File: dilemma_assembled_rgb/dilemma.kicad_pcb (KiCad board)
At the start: 2 copper layers, 106.1 x 95.1 mm, 121 parts, among them J1 USB_C_Receptacle_USB2.0, J102 Serial, J105 Conn_01x04_Female, J113 Cirque, J2 Conn_01x03_Female, J5 Conn_01x02, SW1 SW_Push, SW110 SW_SPST, SW2 SW_Push, SW3002 RotaryEncoder_Switch, U1 RP2040, U2 GD25Q80CEIGR, U3 XC6210B332MR-G, U4 USBLC6-2P6, Y1 Crystal_GND24

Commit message: bat54
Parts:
- added D3: SK6805-EC15, 0xB2_drawings:LED_SK6805-EC15_hole, F.Cu at (137.7, 36.2)
- D101, D102, D103, D104, D105, D106, D107, D108, D109, D110, D111, D112, D113, D114, D115, D116, D117, D3001: footprint Diode_SMD:D_SOD-323 -> local-libraries:D_1206_handsolder_reversible_hole
- J113: moved to B.Cu
- moved J113 22.5 mm to (131.5, 93.6), turned to -90 degrees

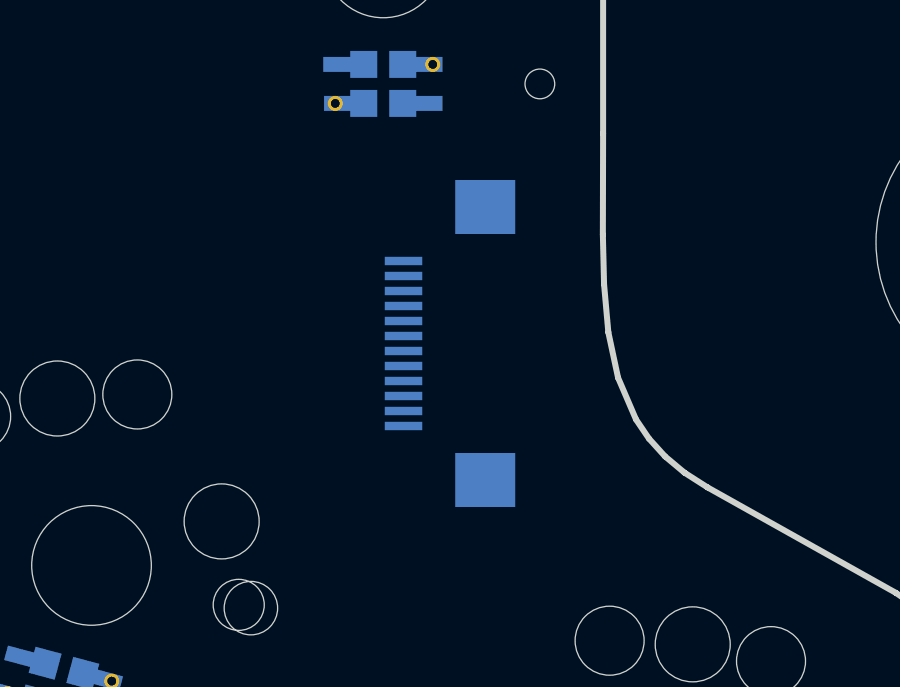
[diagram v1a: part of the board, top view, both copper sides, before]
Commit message: switch rgb to smd connectors
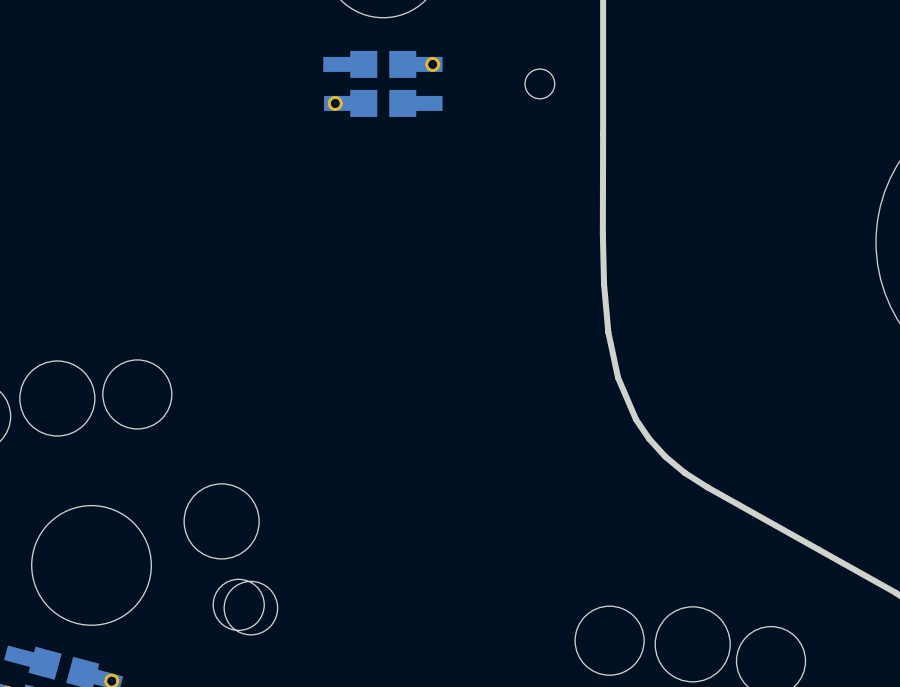
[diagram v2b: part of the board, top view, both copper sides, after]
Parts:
- removed J113: Cirque, local-libraries:FPC-SMD_FPC05012-09200-.5mm

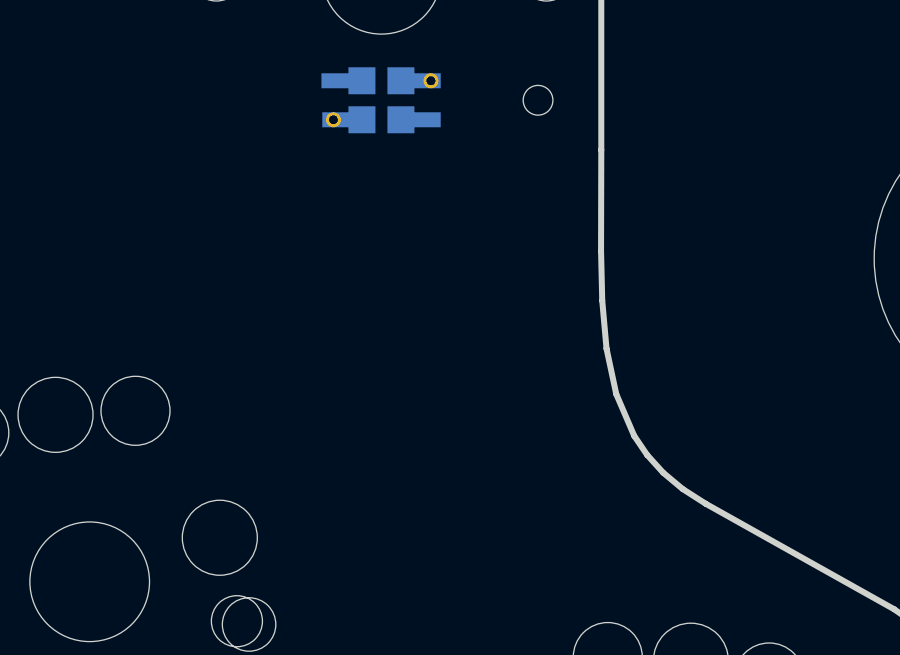
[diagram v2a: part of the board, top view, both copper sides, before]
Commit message: flip debug headers
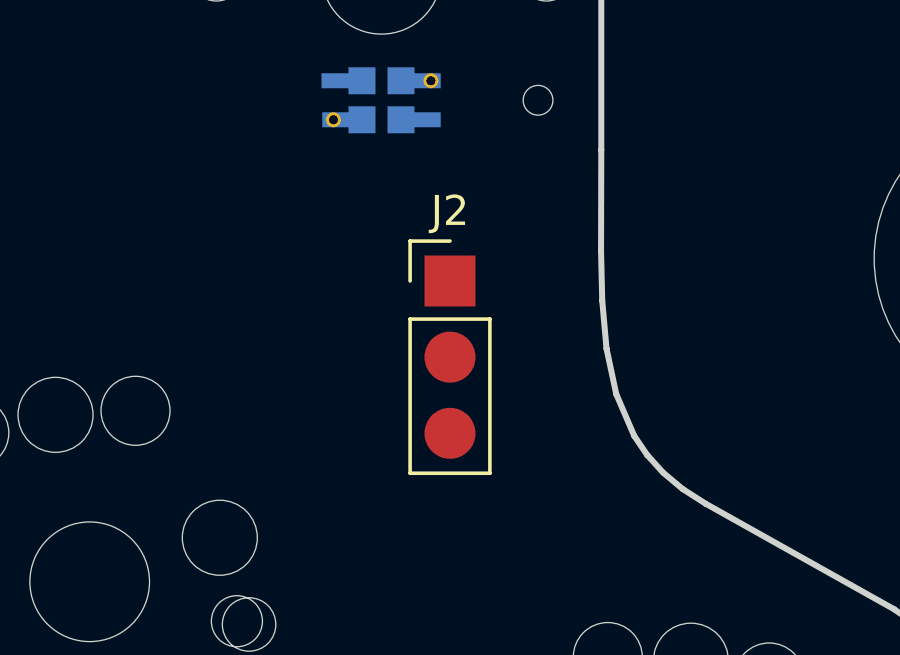
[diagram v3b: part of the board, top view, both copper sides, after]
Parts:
- added J2: Conn_01x03_Female, local-libraries:PinHeader_1x03_P2.54mm_Vertical_smd, F.Cu at (131.7, 91.0)
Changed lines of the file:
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@@
     (fp_line (start 1.3 -0.2) (end 1.3 7.75) (layer "B.SilkS") (width 0.12))
     (fp_line (start -1.299921 -0.198003) (end -1.299921 7.751997) (layer "B.SilkS") (width 0.12))
-    (fp_arc (start -1.299921 -0.198003) (mid -0.00092 -1.448967) (end 1.3 -0.2) (layer "B.SilkS") (width 0.12))
-    (fp_arc (start 1.3 7.75) (mid 0.000999 9.000965) (end -1.299921 7.751997) (layer "B.SilkS") (width 0.12))
+    (fp_arc (start -1.299921 -0.198003) (mid -0.00092 -1.448968) (end 1.3 -0.2) (layer "B.SilkS") (width 0.12))
+    (fp_arc (start 1.3 7.75) (mid 0.000999 9.000966) (end -1.299921 7.751997) (layer "B.SilkS") (width 0.12))
     (fp_line (start 1.314577 -0.199039) (end 1.314577 7.751997) (layer "F.SilkS") (width 0.12))
     (fp_line (start -1.285344 -0.201036) (end -1.285344 7.75) (layer "F.SilkS") (width 0.12))
@@
     (pad "" np_thru_hole oval (at 0 0 180) (size 6.5 3) (drill oval 6.5 3) (layers F&B.Cu *.Mask))
   )
+  (footprint "local-libraries:PinHeader_1x03_P2.54mm_Vertical_smd" (layer "F.Cu")
+    (at 131.71 90.97)
+    (descr "Through hole straight pin header, 1x03, 2.54mm pitch, single row")
+    (tags "Through hole pin header THT 1x03 2.54mm single row")
+    (property "Sheetfile" "dilemma.kicad_sch")
+    (property "Sheetname" "")
+    (attr through_hole)
+    (fp_text reference "J2" (at 0 -2.33) (layer "F.SilkS")
+      (effects (font (size 1 1) (thickness 0.15)))
+    )
+    (fp_text value "Conn_01x03_Female" (at 0 7.41) (layer "F.Fab")
+      (effects (font (size 1 1) (thickness 0.15)))
+    )
+    (fp_text user "${REFERENCE}" (at 0 2.54 90) (layer "F.Fab")
+      (effects (font (size 1 1) (thickness 0.15)))
+    )
+    (fp_line (start -1.33 6.41) (end 1.33 6.41) (layer "F.SilkS") (width 0.12))
+    (fp_line (start -1.33 0) (end -1.33 -1.33) (layer "F.SilkS") (width 0.12))
+    (fp_line (start -1.33 1.27) (end -1.33 6.41) (layer "F.SilkS") (width 0.12))
+    (fp_line (start -1.33 1.27) (end 1.33 1.27) (layer "F.SilkS") (width 0.12))
+    (fp_line (start -1.33 -1.33) (end 0 -1.33) (layer "F.SilkS") (width 0.12))
+    (fp_line (start 1.33 1.27) (end 1.33 6.41) (layer "F.SilkS") (width 0.12))
+    (fp_line (start -1.8 6.85) (end 1.8 6.85) (layer "F.CrtYd") (width 0.05))
+    (fp_line (start -1.8 -1.8) (end -1.8 6.85) (layer "F.CrtYd") (width 0.05))
+    (fp_line (start 1.8 -1.8) (end -1.8 -1.8) (layer "F.CrtYd") (width 0.05))
+    (fp_line (start 1.8 6.85) (end 1.8 -1.8) (layer "F.CrtYd") (width 0.05))
+    (fp_line (start -0.635 -1.27) (end 1.27 -1.27) (layer "F.Fab") (width 0.1))
+    (fp_line (start -1.27 -0.635) (end -0.635 -1.27) (layer "F.Fab") (width 0.1))
+    (fp_line (start 1.27 6.35) (end -1.27 6.35) (layer "F.Fab") (width 0.1))
+    (fp_line (start 1.27 -1.27) (end 1.27 6.35) (layer "F.Fab") (width 0.1))
+    (fp_line (start -1.27 6.35) (end -1.27 -0.635) (layer "F.Fab") (width 0.1))
+    (pad "1" smd rect (at 0 0) (size 1.7 1.7) (layers "F.Cu" "F.Paste" "F.Mask")
+      (net 14 "GND") (pinfunction "Pin_1") (pintype "passive"))
+    (pad "2" smd oval (at 0 2.54) (size 1.7 1.7) (layers "F.Cu" "F.Paste" "F.Mask")
+      (net 57 "+3V3") (pinfunction "Pin_2") (pintype "passive"))
+    (pad "3" smd oval (at 0 5.08) (size 1.7 1.7) (layers "F.Cu" "F.Paste" "F.Mask")
+      (net 56 "RGB") (pinfunction "Pin_3") (pintype "passive"))
+    (model "${KICAD6_3DMODEL_DIR}/Connector_PinHeader_2.54mm.3dshapes/PinHeader_1x03_P2.54mm_Vertical.wrl"
+      (offset (xyz 0 0 0))
+      (scale (xyz 1 1 1))
+      (rotate (xyz 0 0 0))
+    )
+  )
   (footprint "Capacitor_SMD:C_0402_1005Metric" (layer "F.Cu")

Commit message: cleanup
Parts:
- removed D101, D102, D103, D104, D105, D106, D107, D108, D109, D110, D111, D112, D113, D114, D115, D116, D117, D3001: D, local-libraries:D_1206_handsolder_reversible_hole
- added D10: SK6805-EC15, 0xB2_drawings:LED_SK6805-EC15_hole, F.Cu at (291.8, 15.6)
- added D13: SK6805-EC15, 0xB2_drawings:LED_SK6805-EC15_hole, F.Cu at (299.4, 15.6)
- added D14: SK6805-EC15, 0xB2_drawings:LED_SK6805-EC15_hole, F.Cu at (295.6, 19.4)
- added D17: SK6805-EC15, 0xB2_drawings:LED_SK6805-EC15_hole, F.Cu at (303.2, 15.6)
- added D20: SK6805-EC15, 0xB2_drawings:LED_SK6805-EC15_hole, F.Cu at (299.4, 19.4)
- added D23: SK6805-EC15, 0xB2_drawings:LED_SK6805-EC15_hole, F.Cu at (291.8, 23.2)
- added D26: SK6805-EC15, 0xB2_drawings:LED_SK6805-EC15_hole, F.Cu at (291.8, 19.4)
- added D29: SK6805-EC15, 0xB2_drawings:LED_SK6805-EC15_hole, F.Cu at (295.6, 15.6)
- added D6: SK6805-EC15, 0xB2_drawings:LED_SK6805-EC15_hole, F.Cu at (295.6, 23.2)
- added D9: SK6805-EC15, 0xB2_drawings:LED_SK6805-EC15_hole, F.Cu at (291.8, 27.0)
- added J113: Cirque, local-libraries:FPC-SMD_FPC05012-09200-.5mm, F.Cu at (282.2, 29.9)
- SW3002: footprint local-libraries:RotaryEncoder_Alps_EC11E-Switch_Vertical_H20mm_roundholes -> local-libraries:RotaryEncoder_Alps_EC11E-Switch_Vertical_H20mm_holes
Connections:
- D46 pad 3: Net-(D46-Pad3) -> unconnected-(D46-Pad3)

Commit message: cleanup
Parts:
- removed D10, D13, D14, D17, D20, D23, D26, D29, D5, D6, D9: SK6805-EC15, 0xB2_drawings:LED_SK6805-EC15_hole
- D11, D12, D15, D16, D18, D19: value SK6805-EC15 -> NA_SK6805-hole
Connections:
- D1 pad 1: Net-(D1-Pad1) -> (no net)
- D1 pad 2: /LED -> (no net)
- D30 pad 1: UNDER_RGB -> RGB
- R1 pad 2: Net-(D1-Pad1) -> unconnected-(R1-Pad2)
